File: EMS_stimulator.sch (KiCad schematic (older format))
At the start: 98 parts, among them IC1 MCP73832, IC2 TPS78230, IC3 MIC5501, IC4 MAX5820, IC5 INA180, IC6 TLV3201, IC7 MAX9619, IC8 TS880ILT, J1 USB_B_micro, P1 TAG connector 2x3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

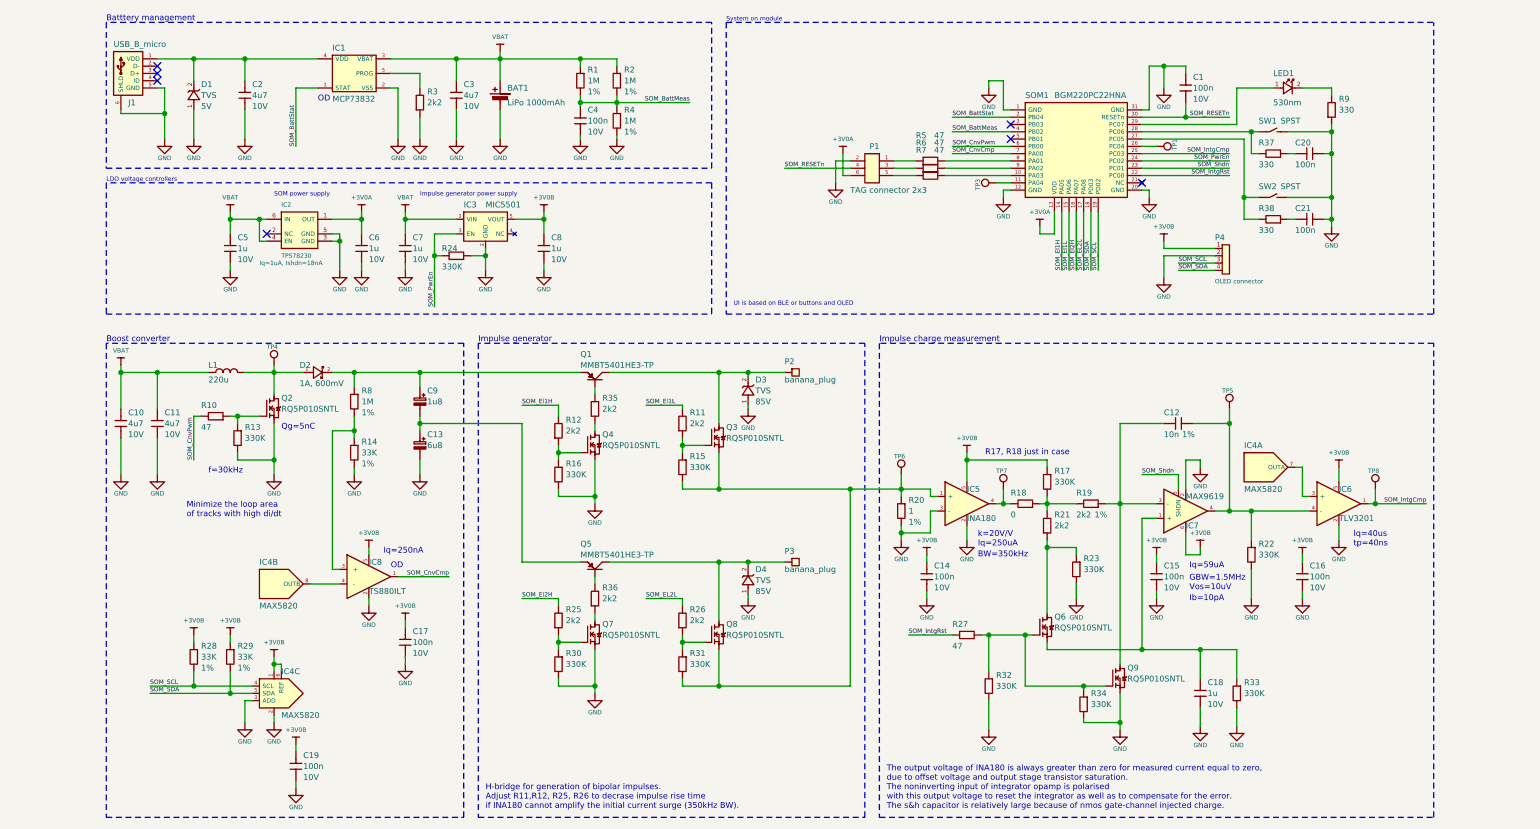
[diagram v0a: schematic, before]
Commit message: Update schematic with switches neccesary to generate two different voltages on separate capacitors.
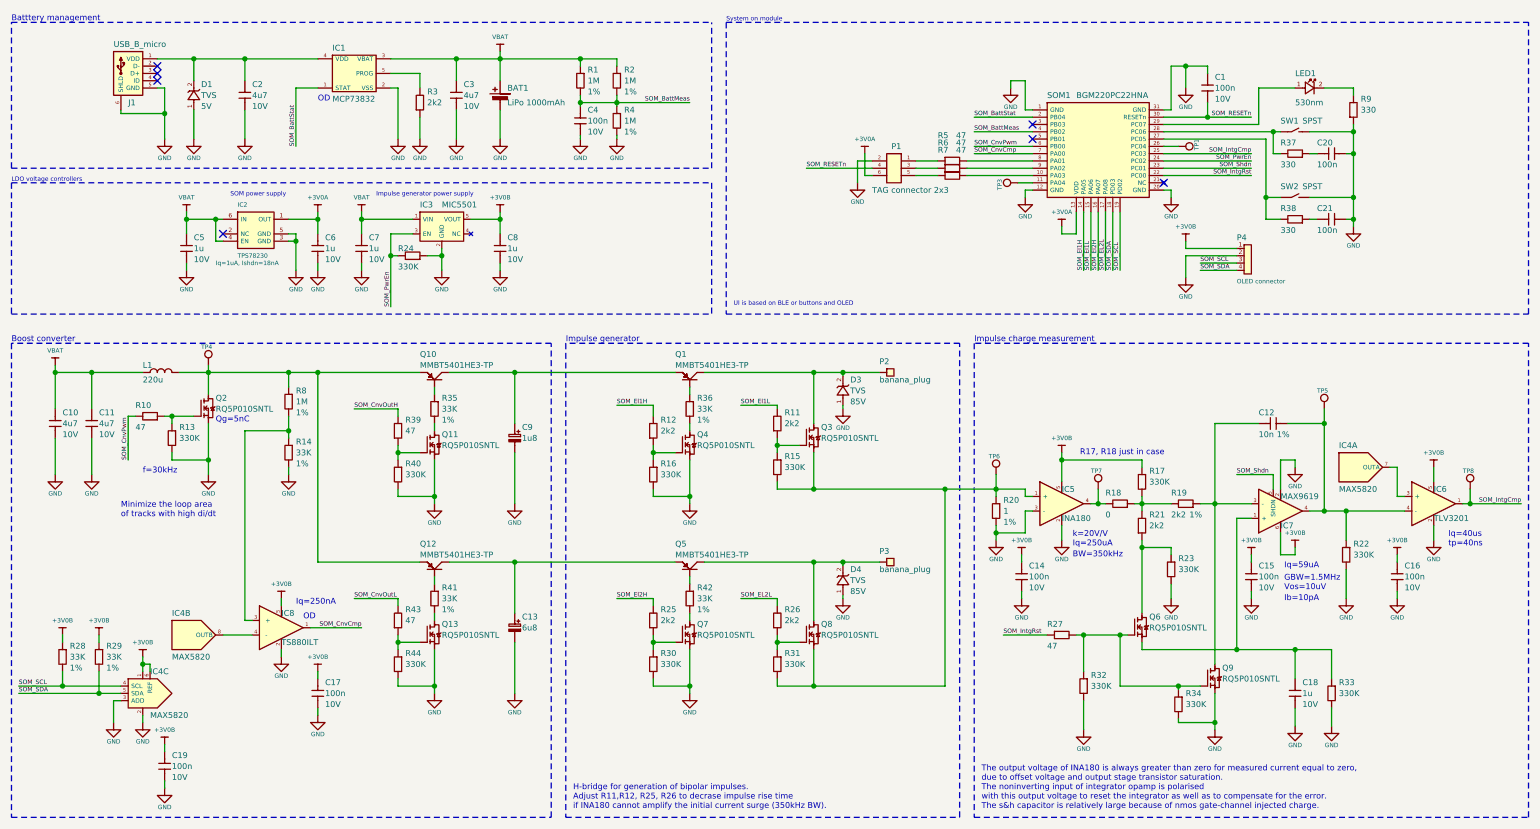
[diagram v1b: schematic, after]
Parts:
- removed D2: 1A, 600mV, WL_diodes:SOD-123FL, symbol WL_diodes:Schottky_diode
- added Q10, Q12: PNP_BEC, WL_transistors_smd:SOT-23-3, symbol WL_transistors:PNP_BEC
- added Q11, Q13: NMOS, WL_transistors_smd:SOT-346, symbol WL_transistors:NMOS_GSD
- added R39, R43: 47, WL_passives:R0402, symbol WL_passive:resistor
- added R40, R44: 330K, WL_passives:R0402, symbol WL_passive:resistor
- added R41, R42: 33K, WL_passives:R0402, symbol WL_passive:resistor
- R35, R36: value 2k2 -> 33K; manf# RC0402FR-072K2P -> CRCW040233K0FKEDC
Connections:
- net GND: now also C9.2 (-), Q11.2 (S), Q13.2 (S), R40.2, R44.2
- net at L1.2, Q2.3 (D), TP4.1: now also R8.1, Q10.2 (E), Q12.2 (E)
- net at C9.1 (+), Q1.2 (E): now also Q10.3 (C); no longer R8.1
- net at C13.1 (+), Q5.2 (E): now also Q12.3 (C); no longer C9.2 (-)
- net at Q1.1 (B): now also R36.1; no longer R35.2
- net at R35.1: now also Q10.1 (B); no longer Q4.3 (D)
- net at Q7.3 (D): now also R42.2; no longer R36.1
- net at Q5.1 (B): now also R42.1; no longer R36.2
- new net: Q11.1 (G), R39.1, R40.1
- new net: Q11.3 (D), R35.2
- new net: Q12.1 (B), R41.1
- new net: Q13.1 (G), R43.1, R44.1
- new net: Q13.3 (D), R41.2
- new net: Q4.3 (D), R36.2
- new net SOM_CnvOutH: R39.2
- new net SOM_CnvOutL: R43.2
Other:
- moved on the sheet: C1, C10, C11, C12, C13, C14, C15, C16, C17, C18, C19, C20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
